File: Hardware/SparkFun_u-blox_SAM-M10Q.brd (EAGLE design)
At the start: 40.6 x 40.6 mm, 76 parts, among them J1 Qwiic Right Angle, J2 Qwiic Right Angle, J4 BOOT, U1 U-BLOX_SAM_M10Q-00B

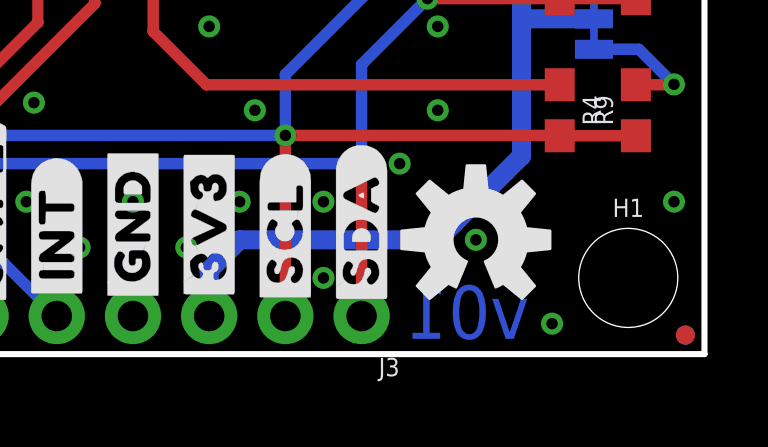
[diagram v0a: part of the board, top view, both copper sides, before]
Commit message: Update for v10, Panelize. Add measures.
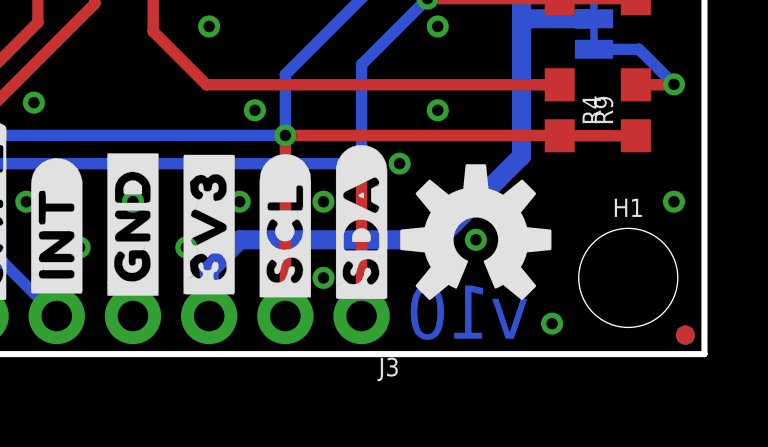
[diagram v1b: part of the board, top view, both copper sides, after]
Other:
- board text added: "All units in inches"
- board text added: "v10"
- board text removed: "v01"
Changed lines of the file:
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@@
 <drawing>
 <settings>
-<setting alwaysvectorfont="yes"/>
+<setting alwaysvectorfont="no"/>
 <setting verticaltext="up"/>
 </settings>
@@
 <wire x1="12.7" y1="38.1" x2="27.94" y2="38.1" width="0.1778" layer="22"/>
 <wire x1="27.94" y1="38.1" x2="27.94" y2="40.64" width="0.1778" layer="22"/>
-<text x="34.798" y="0.508" size="1.778" layer="16" font="vector" ratio="15" rot="MR0">v01</text>
+<text x="34.798" y="0.508" size="1.778" layer="16" font="vector" ratio="15" rot="MR0">v10</text>
 <text x="48.768" y="-8.89" size="1.778" layer="51" font="vector">Alex Brudner</text>
 <text x="21.59" y="-12.192" size="1.778" layer="51" font="vector">Based on the SAM_M8Q by N. Seidle &amp; E. Santistevan</text>
+<dimension x1="0" y1="0" x2="0" y2="40.64" x3="-25.654" y3="20.32" textsize="1.778" layer="47" dtype="vertical" unit="inch"/>
+<dimension x1="0" y1="0" x2="2.54" y2="2.54" x3="-1.27" y3="1.27" textsize="1.778" layer="47" dtype="vertical" unit="inch"/>
+<dimension x1="0" y1="0" x2="13.97" y2="39.37" x3="-22.606" y3="19.685" textsize="1.778" layer="47" dtype="vertical" unit="inch"/>
+<dimension x1="0" y1="0" x2="2.54" y2="38.1" x3="-19.558" y3="19.05" textsize="1.778" layer="47" dtype="vertical" unit="inch"/>
+<dimension x1="0" y1="0" x2="5.08" y2="20.32" x3="-16.51" y3="10.16" textsize="1.778" layer="47" dtype="vertical" unit="inch"/>
+<dimension x1="0" y1="0" x2="20.32" y2="20.32" x3="-13.208" y3="10.16" textsize="1.778" layer="47" dtype="vertical" unit="inch"/>
+<dimension x1="0" y1="0" x2="11.43" y2="1.27" x3="-4.318" y3="0.635" textsize="1.778" layer="47" dtype="vertical" unit="inch"/>
+<dimension x1="0" y1="40.64" x2="40.64" y2="40.64" x3="20.32" y3="68.834" textsize="1.778" layer="47" dtype="horizontal" unit="inch"/>
+<dimension x1="0" y1="40.64" x2="38.1" y2="38.1" x3="19.05" y3="65.786" textsize="1.778" layer="47" dtype="horizontal" unit="inch"/>
+<dimension x1="0" y1="40.64" x2="35.56" y2="20.32" x3="17.78" y3="62.738" textsize="1.778" layer="47" dtype="horizontal" unit="inch"/>
+<dimension x1="0" y1="40.64" x2="20.32" y2="20.32" x3="10.16" y3="59.69" textsize="1.778" layer="47" dtype="horizontal" unit="inch"/>
+<dimension x1="0" y1="40.64" x2="13.97" y2="39.37" x3="6.985" y3="56.642" textsize="1.778" layer="47" dtype="horizontal" unit="inch"/>
+<dimension x1="0" y1="40.64" x2="11.43" y2="1.27" x3="5.715" y3="53.34" textsize="1.778" layer="47" dtype="horizontal" unit="inch"/>
+<dimension x1="0" y1="40.64" x2="5.08" y2="20.32" x3="2.54" y3="49.784" textsize="1.778" layer="47" dtype="horizontal" unit="inch"/>
+<dimension x1="0" y1="40.64" x2="2.54" y2="38.1" x3="1.27" y3="42.672" textsize="1.778" layer="47" dtype="horizontal" unit="inch"/>
+<text x="-23.622" y="45.466" size="1.778" layer="47" font="vector">All units in inches</text>
 </plain>
 <attributes>
@@
 <element name="FRAME1" library="SparkFun-Aesthetics" package="CREATIVE_COMMONS" value="FRAME-LETTER" x="21.59" y="-8.89" smashed="yes">
 <attribute name="DESIGNER" value="Alex Brudner" x="21.59" y="-8.89" size="1.778" layer="27" display="off"/>
-<attribute name="REV" value="v01" x="21.59" y="-8.89" size="1.778" layer="27" display="off"/>
+<attribute name="REV" value="v10" x="21.59" y="-8.89" size="1.778" layer="27" display="off"/>
 </element>
 <element name="FD1" library="SparkFun-Aesthetics" package="FIDUCIAL-MICRO" value="FIDUCIALUFIDUCIAL" x="40.005" y="0.635" smashed="yes" rot="MR0"/>

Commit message: Update post design review.
Swap for updated reflowable battery.
Adjust note for battery accordingly.
Add qwiic symbol in schematic, replacing silk only on board.
Expand t/b keepout under M10Q.
Swap SCL/SDA silk so they are on the correct pins.
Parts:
- removed U$39: (no value), output:SAM_M10Q0
- added LOGO3: QWIIC_LOGO_CONNECTOR, SparkFun-Aesthetics:QWIIC_5.5MM
- BT1: device SparkFun-Batteries:ML414H_IV01E -> SparkFun-Batteries:MS421R_IV03E
- U$18: device output:U#BLOX19 -> output:U#BLOX11
- U$2: device SparkFun-Aesthetics:QWIIC_5MM -> output:SAM#M10Q11
- U$32: device output:SAM_M10Q0 -> output:SAM#M10Q12
- U$38: device output:U#BLOX19 -> output:U#BLOX12
- moved U$32 21.2 mm to (20.3, 11.9), flipped to the bottom
- moved U$2 12.8 mm to (34.5, 27.9)
- moved U$24 2.54 mm to (29.2, 4.06)
- moved U$25 2.54 mm to (29.2, 4.06)
- moved U$26 2.54 mm to (26.7, 4.19)
- moved U$27 2.54 mm to (26.7, 4.19)
- moved U$18 0.13 mm to (34.4, 30.0)
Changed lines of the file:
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@@
 <layer number="28" name="bValues" color="7" fill="1" visible="no" active="yes"/>
 <layer number="29" name="tStop" color="7" fill="3" visible="yes" active="yes"/>
-<layer number="30" name="bStop" color="7" fill="6" visible="no" active="yes"/>
-<layer number="31" name="tCream" color="7" fill="4" visible="no" active="yes"/>
+<layer number="30" name="bStop" color="7" fill="6" visible="yes" active="yes"/>
+<layer number="31" name="tCream" color="7" fill="4" visible="yes" active="yes"/>
 <layer number="32" name="bCream" color="7" fill="5" visible="no" active="yes"/>
 <layer number="33" name="tFinish" color="6" fill="3" visible="no" active="yes"/>
@@
 <element name="LOGO1" library="SparkFun-Aesthetics" package="OSHW-LOGO-M" value="OSHW-LOGOM" x="33.02" y="3.81" smashed="yes"/>
 <element name="LOGO2" library="SparkFun-Aesthetics" package="SFE_LOGO_NAME_FLAME_.2" value="SFE_LOGO_NAME_FLAME.2_INCH" x="20.32" y="20.32" smashed="yes" rot="MR0"/>
-<element name="BT1" library="SparkFun-Batteries" package="ML414H_IV01E" value="6.8MM_COIN_CELL" x="4.572" y="31.496" smashed="yes" rot="R180">
+<element name="BT1" library="SparkFun-Batteries" package="MS421R_IV03E" value="6.8MM_COIN_CELL" x="4.572" y="31.496" smashed="yes" rot="R180">
 <attribute name="NAME" x="5.588" y="28.575" size="0.381" layer="25" rot="R180"/>
-<attribute name="PROD_ID" value="BATT-14267" x="10.922" y="27.686" size="1.778" layer="27" rot="R180" display="off"/>
+<attribute name="PROD_ID" value="BAT-16685" x="10.922" y="27.686" size="1.778" layer="27" rot="R180" display="off"/>
 <attribute name="VALUE" x="5.588" y="34.798" size="0.381" layer="27" rot="R180"/>
 </element>
@@
 </element>
 <element name="U$1" library="SparkFun-Aesthetics" package="SFE_LOGO_FLAME_STOP_.1" value="" x="7.112" y="2.54" smashed="yes"/>
-<element name="U$2" library="SparkFun-Aesthetics" package="QWIIC_5MM" value="" x="37.592" y="15.494" smashed="yes"/>
 <element name="U$3" library="output" package="BLK4" value="" x="11.938" y="39.37" smashed="yes" rot="R90"/>
 <element name="U$4" library="output" package="BLK4" value="" x="11.938" y="39.37" smashed="yes" rot="MR90"/>
@@
 <element name="U$22" library="output" package="#3V3#0" value="" x="24.13" y="4.318" smashed="yes" rot="R90"/>
 <element name="U$23" library="output" package="#3V3#0" value="" x="24.13" y="4.318" smashed="yes" rot="MR90"/>
-<element name="U$24" library="output" package="#SCL#6" value="" x="26.67" y="4.064" smashed="yes" rot="R90"/>
-<element name="U$25" library="output" package="#SCL#6" value="" x="26.67" y="4.064" smashed="yes" rot="MR90"/>
-<element name="U$26" library="output" package="#SDA#7" value="" x="29.21" y="4.191" smashed="yes" rot="R90"/>
-<element name="U$27" library="output" package="#SDA#7" value="" x="29.21" y="4.191" smashed="yes" rot="MR90"/>
+<element name="U$24" library="output" package="#SCL#6" value="" x="29.21" y="4.064" smashed="yes" rot="R90"/>
+<element name="U$25" library="output" package="#SCL#6" value="" x="29.21" y="4.064" smashed="yes" rot="MR90"/>
+<element name="U$26" library="output" package="#SDA#7" value="" x="26.67" y="4.191" smashed="yes" rot="R90"/>
+<element name="U$27" library="output" package="#SDA#7" value="" x="26.67" y="4.191" smashed="yes" rot="MR90"/>
 <element name="U$28" library="output" package="#INT#8" value="" x="19.05" y="4.064" smashed="yes" rot="R90"/>
 <element name="U$29" library="output" package="#INT#8" value="" x="19.05" y="4.064" smashed="yes" rot="MR90"/>
@@
 <element name="U$37" library="output" package="##SAFE##16" value="" x="16.51" y="4.699" smashed="yes" rot="MR90"/>
 <element name="U$31" library="SparkFun-Aesthetics" package="SFE_LOGO_NAME_.1" value="" x="20.32" y="31.496" smashed="yes"/>
-<element name="U$18" library="output" package="U#BLOX19" value="" x="34.544" y="29.972" smashed="yes"/>
-<element name="U$32" library="output" package="SAM_M10Q0" value="" x="34.798" y="27.432" smashed="yes"/>
-<element name="U$38" library="output" package="U#BLOX19" value="" x="20.32" y="14.224" smashed="yes" rot="MR0"/>
-<element name="U$39" library="output" package="SAM_M10Q0" value="" x="20.32" y="11.684" smashed="yes" rot="MR0"/>
 <element name="U$42" library="output" package="#PWRLED#0" value="" x="6.858" y="12.954" smashed="yes" rot="MR0"/>
 <element name="U$40" library="output" package="#PPSLED#0" value="" x="6.731" y="8.382" smashed="yes" rot="MR0"/>
 <element name="U$41" library="output" package="#I2CPUR#0" value="" x="35.433" y="11.176" smashed="yes" rot="MR90"/>
+<element name="LOGO3" library="SparkFun-Aesthetics" package="QWIIC_5.5MM" value="QWIIC_LOGO_CONNECTOR" x="37.338" y="15.494" smashed="yes"/>
+<element name="U$2" library="output" package="SAM#M10Q11" value="" x="34.544" y="27.94" smashed="yes"/>
+<element name="U$18" library="output" package="U#BLOX11" value="" x="34.417" y="29.972" smashed="yes"/>
+<element name="U$32" library="output" package="SAM#M10Q12" value="" x="20.32" y="11.938" smashed="yes" rot="MR0"/>
+<element name="U$38" library="output" package="U#BLOX12" value="" x="20.32" y="14.224" smashed="yes" rot="MR0"/>
 </elements>
 <signals>

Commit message: Rework paste for DFM experiment.
Move original panel into 100_paste folder.
Repanelize with quad box paste and put into quad_paste folder.
Update library to have new variant.
Update sch and brd with new part.
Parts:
- U1: value U-BLOX_SAM_M10Q-00B -> U-BLOX_SAM_M10Q-00B_100_PASTE; device u-blox_SAM-M10Q:SAM-M10Q -> u-blox_SAM-M10Q:SAM-M10Q_100PASTE

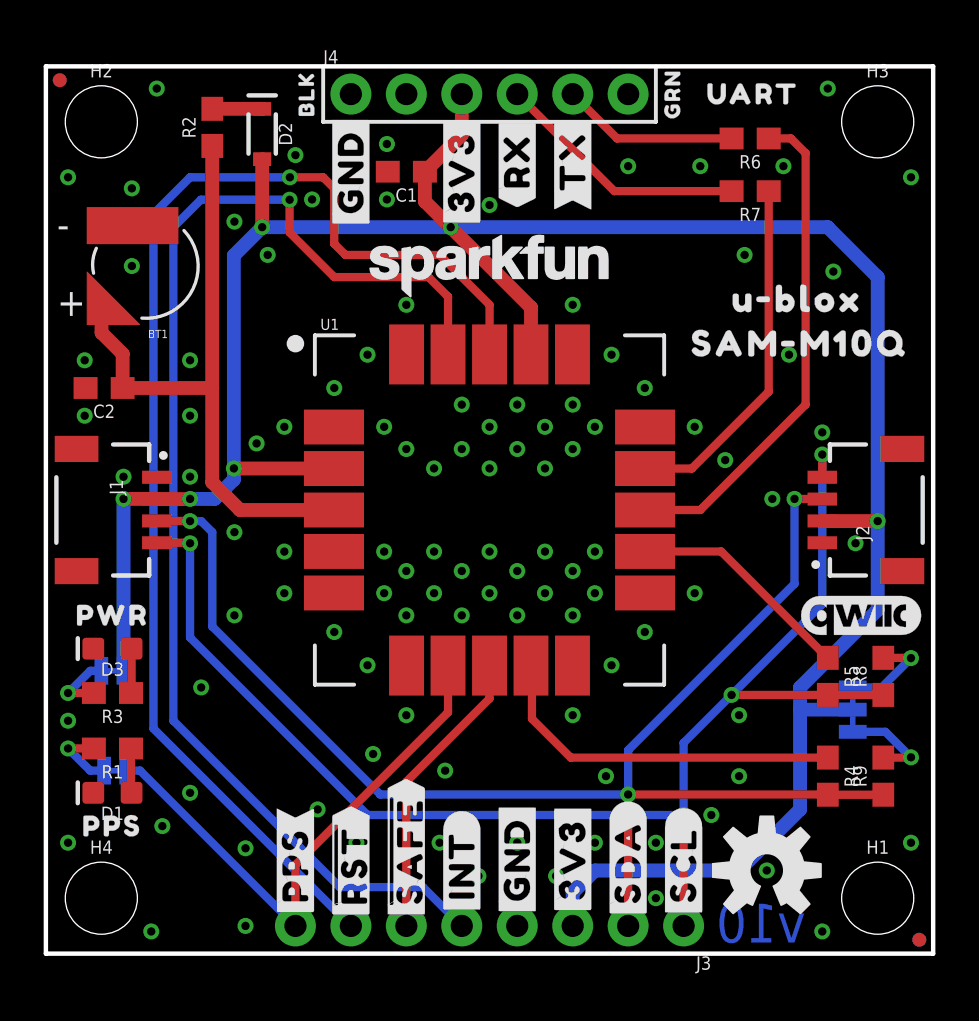
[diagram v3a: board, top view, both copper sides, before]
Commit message: Update for release
Remove quad paste part from lib.
Remove quad paste production folder.
Move 100 paste up one folder.
Update schematic/board for new part.
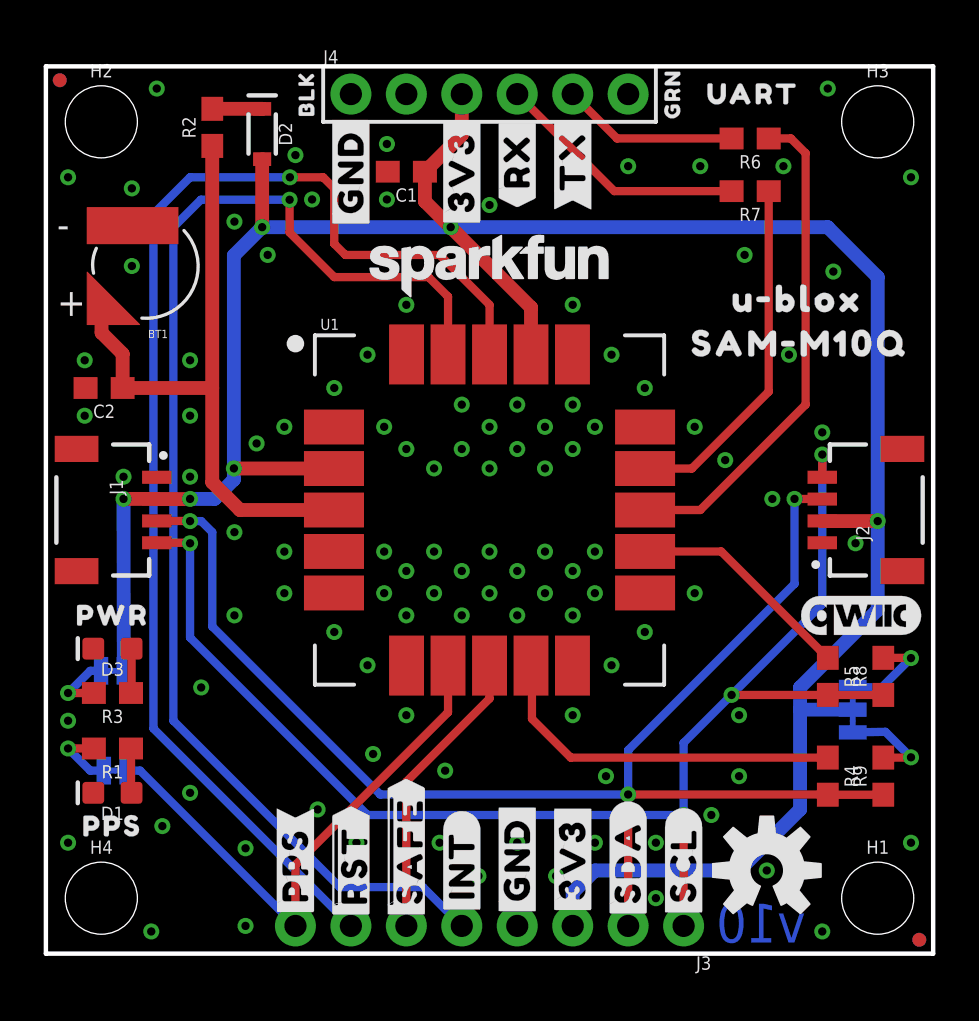
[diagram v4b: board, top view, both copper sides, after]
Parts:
- PPSLED: value (none) -> JUMPER-SMT_2_NC_TRACE_SILK
- R4, R5: value 22 -> 22Ω
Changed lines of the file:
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@@
 <attribute name="VALUE" x="39.116" y="8.128" size="0.6096" layer="27" font="vector" ratio="20" rot="R90" align="top-center"/>
 </element>
-<element name="I2CPUR" library="SparkFun-Jumpers" package="SMT-JUMPER_3_2-NC_TRACE_SILK" value="JUMPER-SMT_3_2-NC_TRACE_SILK" x="36.957" y="11.176" smashed="yes" rot="MR90">
+<element name="I2CPUR" library="SparkFun-Jumpers" package="SMT-JUMPER_3_2-NC_TRACE_SILK" package3d_urn="urn:adsk.eagle:package:39289/1" value="JUMPER-SMT_3_2-NC_TRACE_SILK" x="36.957" y="11.176" smashed="yes" rot="MR90">
 <attribute name="NAME" x="38.1" y="11.176" size="0.6096" layer="26" font="vector" ratio="20" rot="MR90" align="bottom-center"/>
 <attribute name="VALUE" x="35.814" y="11.176" size="0.6096" layer="28" font="vector" ratio="20" rot="MR90" align="top-center"/>
 </element>
-<element name="R4" library="SparkFun-Resistors" package="0603" value="22" x="35.814" y="8.128" smashed="yes" rot="R270">
+<element name="R4" library="SparkFun-Resistors" package="0603" value="22Ω" x="35.814" y="8.128" smashed="yes" rot="R270">
 <attribute name="NAME" x="36.576" y="8.128" size="0.6096" layer="25" font="vector" ratio="20" rot="R270" align="bottom-center"/>
 <attribute name="PROD_ID" value="RES-08698" x="39.624" y="36.068" size="1.778" layer="27" rot="R270" display="off"/>
-<attribute name="VALUE" x="35.052" y="8.128" size="0.6096" layer="27" font="vector" ratio="20" rot="R270" align="top-center"/>
-</element>
-<element name="R5" library="SparkFun-Resistors" package="0603" value="22" x="35.814" y="12.7" smashed="yes" rot="R270">
+<attribute name="VALUE" value="22Ω" x="35.052" y="8.128" size="0.6096" layer="27" font="vector" ratio="20" rot="R270" align="top-center"/>
+</element>
+<element name="R5" library="SparkFun-Resistors" package="0603" value="22Ω" x="35.814" y="12.7" smashed="yes" rot="R270">
 <attribute name="NAME" x="36.576" y="12.7" size="0.6096" layer="25" font="vector" ratio="20" rot="R270" align="bottom-center"/>
 <attribute name="PROD_ID" value="RES-08698" x="35.814" y="44.45" size="1.778" layer="27" rot="R270" display="off"/>
-<attribute name="VALUE" x="35.052" y="12.7" size="0.6096" layer="27" font="vector" ratio="20" rot="R270" align="top-center"/>
+<attribute name="VALUE" value="22Ω" x="35.052" y="12.7" size="0.6096" layer="27" font="vector" ratio="20" rot="R270" align="top-center"/>
 </element>
 <element name="U1" library="u-blox_SAM-M10Q" package="SAM-M10Q_100PASTE" value="U-BLOX_SAM_M10Q-00B_100_PASTE" x="20.32" y="20.32" smashed="yes">
@@
 <attribute name="VALUE" x="3.048" y="8.001" size="0.6096" layer="27" font="vector" ratio="20" rot="R180" align="top-center"/>
 </element>
-<element name="PPSLED" library="SparkFun-Jumpers" package="SMT-JUMPER_2_NC_TRACE_SILK" value="" x="3.175" y="8.382" smashed="yes" rot="MR180">
+<element name="PPSLED" library="SparkFun-Jumpers" package="SMT-JUMPER_2_NC_TRACE_SILK" package3d_urn="urn:adsk.eagle:package:39281/1" value="JUMPER-SMT_2_NC_TRACE_SILK" x="3.175" y="8.382" smashed="yes" rot="MR180">
 <attribute name="NAME" x="3.175" y="7.239" size="0.6096" layer="26" font="vector" ratio="20" rot="MR180" align="bottom-center"/>
 <attribute name="VALUE" x="3.175" y="9.525" size="0.6096" layer="28" font="vector" ratio="20" rot="MR180" align="top-center"/>
@@
 <attribute name="VALUE" x="3.048" y="14.605" size="0.6096" layer="27" font="vector" ratio="20" rot="R180" align="top-center"/>
 </element>
-<element name="PWRLED" library="SparkFun-Jumpers" package="SMT-JUMPER_2_NC_TRACE_SILK" value="JUMPER-SMT_2_NC_TRACE_SILK" x="3.048" y="12.954" smashed="yes" rot="MR180">
+<element name="PWRLED" library="SparkFun-Jumpers" package="SMT-JUMPER_2_NC_TRACE_SILK" package3d_urn="urn:adsk.eagle:package:39281/1" value="JUMPER-SMT_2_NC_TRACE_SILK" x="3.048" y="12.954" smashed="yes" rot="MR180">
 <attribute name="NAME" x="3.048" y="11.811" size="0.6096" layer="26" font="vector" ratio="20" rot="MR180" align="bottom-center"/>
 <attribute name="VALUE" x="3.048" y="14.097" size="0.6096" layer="28" font="vector" ratio="20" rot="MR180" align="top-center"/>
@@
 <wire x1="38.1" y1="19.812" x2="35.568" y2="19.812" width="0.635" layer="1"/>
 <wire x1="35.568" y1="19.812" x2="35.56" y2="19.82" width="0.635" layer="1"/>
-<wire x1="3.556" y1="12.954" x2="3.556" y2="20.828" width="0.635" layer="16"/>
+<wire x1="3.5687" y1="12.954" x2="3.556" y2="20.828" width="0.635" layer="16"/>
 <via x="3.556" y="20.828" extent="1-16" drill="0.381"/>
 <wire x1="3.556" y1="20.828" x2="5.072" y2="20.828" width="0.635" layer="1"/>
@@
 <via x="39.624" y="8.9916" extent="1-16" drill="0.381"/>
 <wire x1="39.624" y1="8.9916" x2="38.4556" y2="10.16" width="0.381" layer="16"/>
-<wire x1="36.957" y1="10.16" x2="38.4556" y2="10.16" width="0.381" layer="16"/>
+<wire x1="36.957" y1="10.1346" x2="38.4556" y2="10.16" width="0.381" layer="16"/>
 </signal>
 <signal name="N$8">
@@
 <via x="39.624" y="13.5382" extent="1-16" drill="0.381"/>
 <wire x1="39.624" y1="13.5382" x2="38.2778" y2="12.192" width="0.381" layer="16"/>
-<wire x1="36.957" y1="12.192" x2="38.2778" y2="12.192" width="0.381" layer="16"/>
+<wire x1="36.957" y1="12.2174" x2="38.2778" y2="12.192" width="0.381" layer="16"/>
 </signal>
 <signal name="SDA_LV">
@@
 <wire x1="11.43" y1="4.064" x2="11.43" y2="1.27" width="0.381" layer="1"/>
 <wire x1="11.43" y1="1.27" x2="4.318" y2="8.382" width="0.381" layer="16"/>
-<wire x1="4.318" y1="8.382" x2="3.683" y2="8.382" width="0.381" layer="16"/>
+<wire x1="4.318" y1="8.382" x2="3.6957" y2="8.382" width="0.381" layer="16"/>
 </signal>
 <signal name="!SAFE">
@@
 <contactref element="PPSLED" pad="1"/>
 <contactref element="R1" pad="2"/>
-<wire x1="2.667" y1="8.382" x2="2.032" y2="8.382" width="0.381" layer="16"/>
+<wire x1="2.6543" y1="8.382" x2="2.032" y2="8.382" width="0.381" layer="16"/>
 <wire x1="2.032" y1="8.382" x2="1.016" y2="9.398" width="0.381" layer="16"/>
 <via x="1.016" y="9.398" extent="1-16" drill="0.381"/>
@@
 <via x="1.016" y="11.938" extent="1-16" drill="0.381"/>
 <wire x1="2.032" y1="12.954" x2="1.016" y2="11.938" width="0.381" layer="16"/>
-<wire x1="2.54" y1="12.954" x2="2.032" y2="12.954" width="0.381" layer="16"/>
+<wire x1="2.5273" y1="12.954" x2="2.032" y2="12.954" width="0.381" layer="16"/>
 </signal>
 <signal name="N$3">
@@
 </board>
 </drawing>
+<compatibility>
+<note version="8.3" severity="warning">
+Since Version 8.3, EAGLE supports URNs for individual library
+assets (packages, symbols, and devices). The URNs of those assets
+will not be understood (or retained) with this version.
+</note>
+<note version="8.3" severity="warning">
+Since Version 8.3, EAGLE supports the association of 3D packages
+with devices in libraries, schematics, and board files. Those 3D
+packages will not be understood (or retained) with this version.
+</note>
+</compatibility>
 </eagle>
